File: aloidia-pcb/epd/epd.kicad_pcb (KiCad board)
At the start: 2 copper layers, 19.6 x 38.6 mm, 20 parts, among them J1 FH12-30S-0.5SH(55), J2 01x08 2.54mm Pin Headers

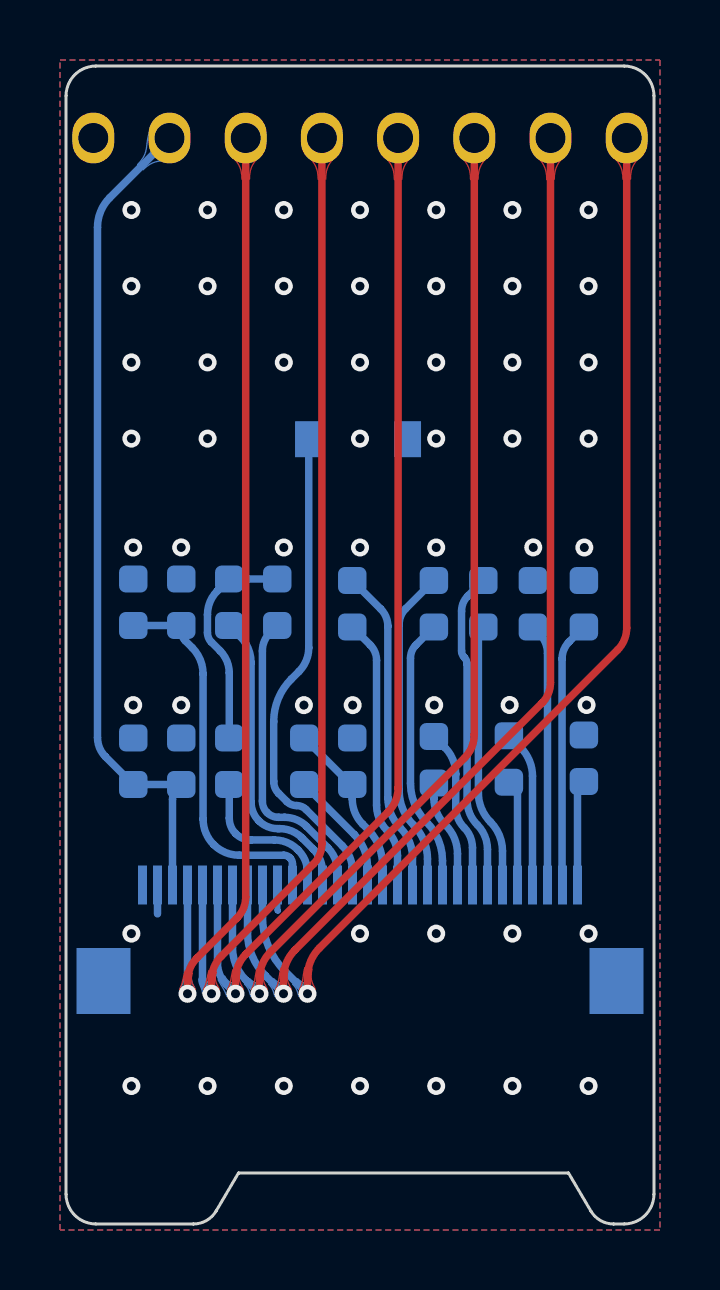
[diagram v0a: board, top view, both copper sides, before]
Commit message: Made e-ink display shorter
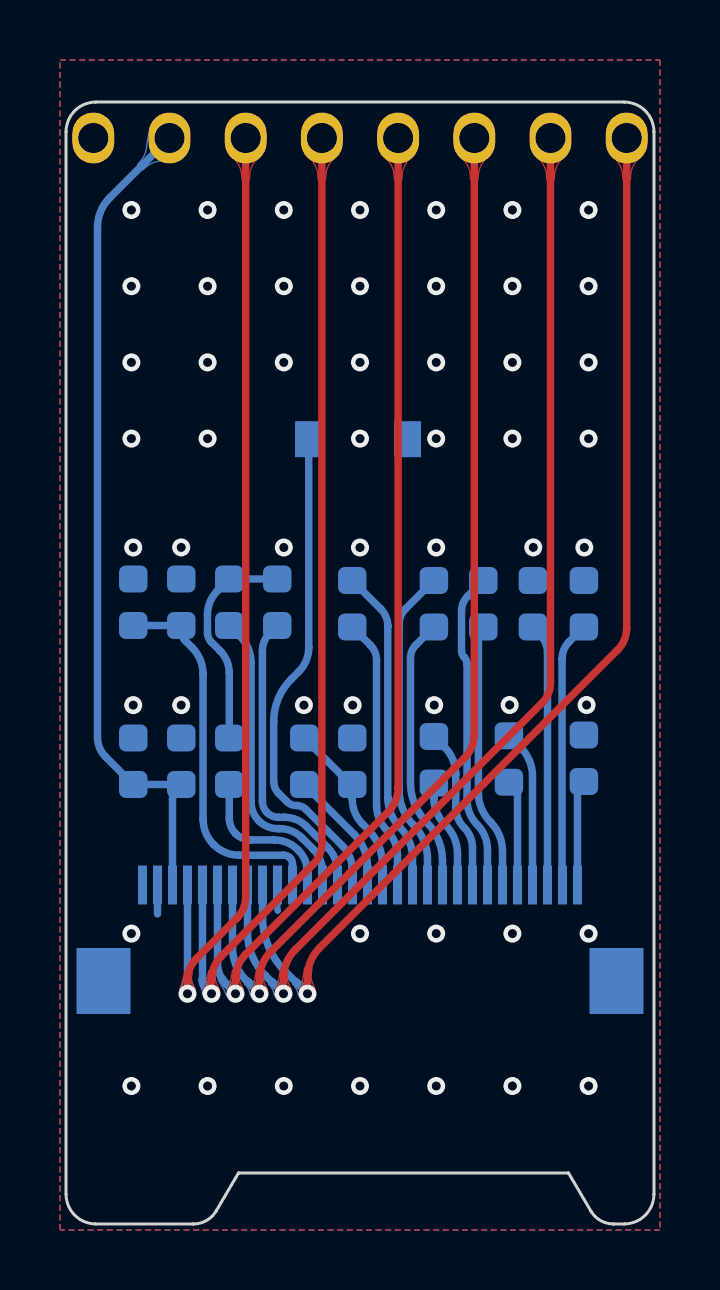
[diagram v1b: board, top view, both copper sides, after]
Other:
- board size 19.6 x 38.6 mm -> 19.6 x 37.4 mm
- board text added: "37.4"
- board text removed: "38.6"
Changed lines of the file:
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@@
     ) (layer "Dwgs.User") (width 0.1) (fill none))
   (gr_rect (start 164.75 96.1) (end 150.75 74.4) (layer "Dwgs.User") (width 0.1) (fill none))
-  (gr_line (start 171 67.95) (end 171 106.45) (layer "Cmts.User") (width 0.15))
-  (gr_line (start 171 67.95) (end 170.5 68.65) (layer "Cmts.User") (width 0.15))
+  (gr_line (start 171 69.15) (end 171 107.65) (layer "Cmts.User") (width 0.15))
+  (gr_line (start 171 69.15) (end 170.5 69.85) (layer "Cmts.User") (width 0.15))
   (gr_line (start 167.55 105.4) (end 167.55 110.2) (layer "Cmts.User") (width 0.08))
   (gr_line (start 167.5 109.5) (end 166.8 110) (layer "Cmts.User") (width 0.15))
@@
   (gr_line (start 171 106.45) (end 170.5 105.75) (layer "Cmts.User") (width 0.15))
   (gr_line (start 148 109.5) (end 148.7 110) (layer "Cmts.User") (width 0.15))
-  (gr_line (start 166.35 67.9) (end 171.65 67.9) (layer "Cmts.User") (width 0.08))
+  (gr_line (start 166.35 69.1) (end 171.65 69.1) (layer "Cmts.User") (width 0.08))
   (gr_line (start 166.35 106.5) (end 171.65 106.5) (layer "Cmts.User") (width 0.08))
-  (gr_line (start 171 67.95) (end 171.5 68.65) (layer "Cmts.User") (width 0.15))
+  (gr_line (start 171 69.15) (end 171.5 69.85) (layer "Cmts.User") (width 0.15))
   (gr_arc (start 166.2 106.5) (mid 165.768984 106.38636) (end 165.45 106.075) (layer "Edge.Cuts") (width 0.1))
   (gr_line (start 153.7 104.8) (end 152.95 106.075) (layer "Edge.Cuts") (width 0.1))
-  (gr_arc (start 166.55 67.9) (mid 167.257107 68.192893) (end 167.55 68.9) (layer "Edge.Cuts") (width 0.1))
+  (gr_arc (start 166.55 69.1) (mid 167.257107 69.392893) (end 167.55 70.1) (layer "Edge.Cuts") (width 0.1))
   (gr_arc (start 148.95 106.5) (mid 148.242893 106.207107) (end 147.95 105.5) (layer "Edge.Cuts") (width 0.1))
-  (gr_line (start 167.55 68.9) (end 167.55 105.5) (layer "Edge.Cuts") (width 0.1))
+  (gr_line (start 167.55 70.1) (end 167.55 105.5) (layer "Edge.Cuts") (width 0.1))
   (gr_line (start 166.55 106.5) (end 166.2 106.5) (layer "Edge.Cuts") (width 0.1))
   (gr_line (start 148.95 106.5) (end 152.2 106.5) (layer "Edge.Cuts") (width 0.1))
@@
   (gr_line (start 153.7 104.8) (end 164.7 104.8) (layer "Edge.Cuts") (width 0.1))
   (gr_arc (start 167.55 105.5) (mid 167.257107 106.207107) (end 166.55 106.5) (layer "Edge.Cuts") (width 0.1))
-  (gr_line (start 148.95 67.9) (end 166.55 67.9) (layer "Edge.Cuts") (width 0.1))
-  (gr_arc (start 147.95 68.9) (mid 148.242893 68.192893) (end 148.95 67.9) (layer "Edge.Cuts") (width 0.1))
+  (gr_line (start 148.95 69.1) (end 166.55 69.1) (layer "Edge.Cuts") (width 0.1))
+  (gr_arc (start 147.95 70.1) (mid 148.242893 69.392893) (end 148.95 69.1) (layer "Edge.Cuts") (width 0.1))
   (gr_line (start 164.7 104.8) (end 165.45 106.075) (layer "Edge.Cuts") (width 0.1))
-  (gr_line (start 147.95 105.5) (end 147.95 68.9) (layer "Edge.Cuts") (width 0.1))
+  (gr_line (start 147.95 105.5) (end 147.95 70.1) (layer "Edge.Cuts") (width 0.1))
   (gr_text "CS" (at 159.02 71.8 270) (layer "B.SilkS")
     (effects (font (size 1 1) (thickness 0.15)) (justify right mirror))
@@
     (effects (font (size 1 1) (thickness 0.15)))
   )
-  (gr_text "38.6" (at 172.15 88.25 90) (layer "Cmts.User")
+  (gr_text "37.4" (at 172.15 88.25 90) (layer "Cmts.User")
     (effects (font (size 1 1) (thickness 0.15)))
   )
